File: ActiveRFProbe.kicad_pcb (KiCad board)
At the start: 2 copper layers, 49 x 22 mm, 40 parts, among them J1 Conn_01x01, J16 Conn_01x01, J17 Conn_01x01, J18 Conn_01x01, J19 Conn_01x01, J2 Conn_01x01, J20 Conn_01x01, J21 Conn_01x01, J22 Conn_01x01, J23 Conn_01x01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

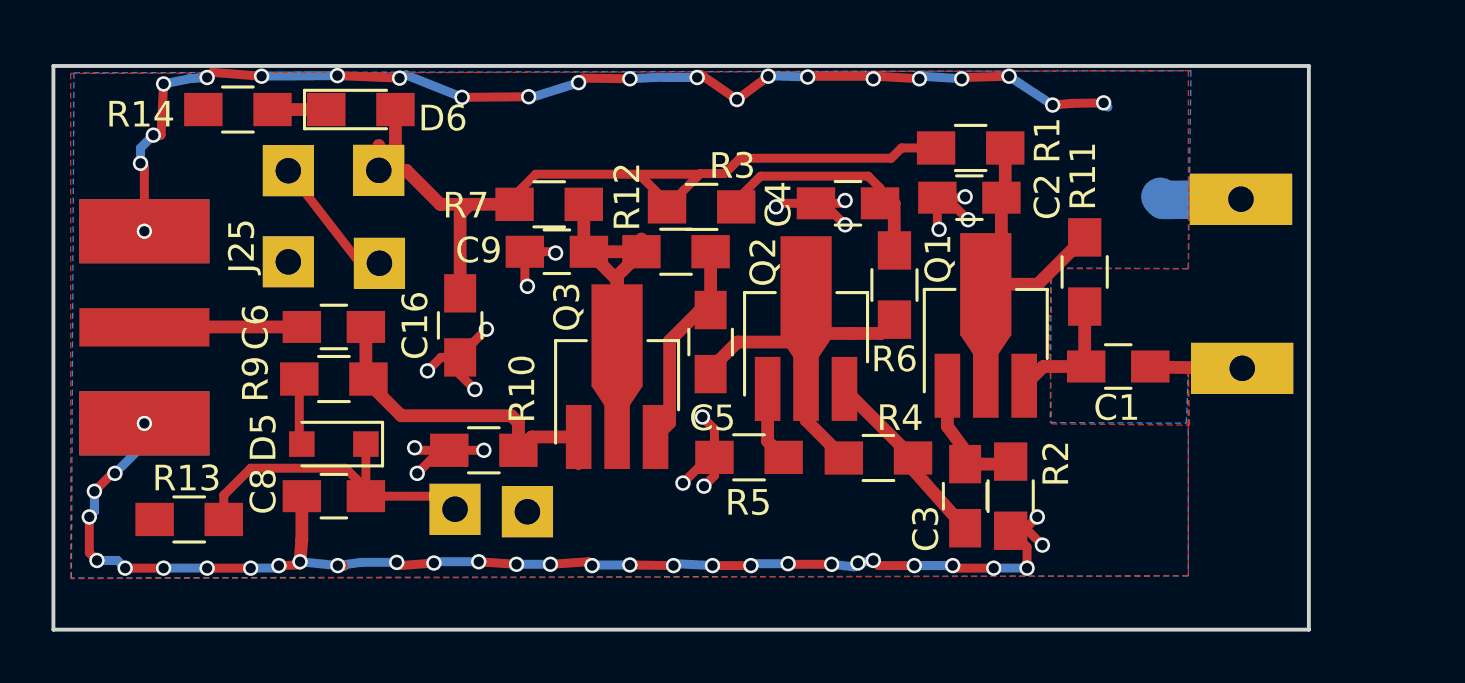
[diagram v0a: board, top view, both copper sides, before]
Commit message: Changed to 2SC3356
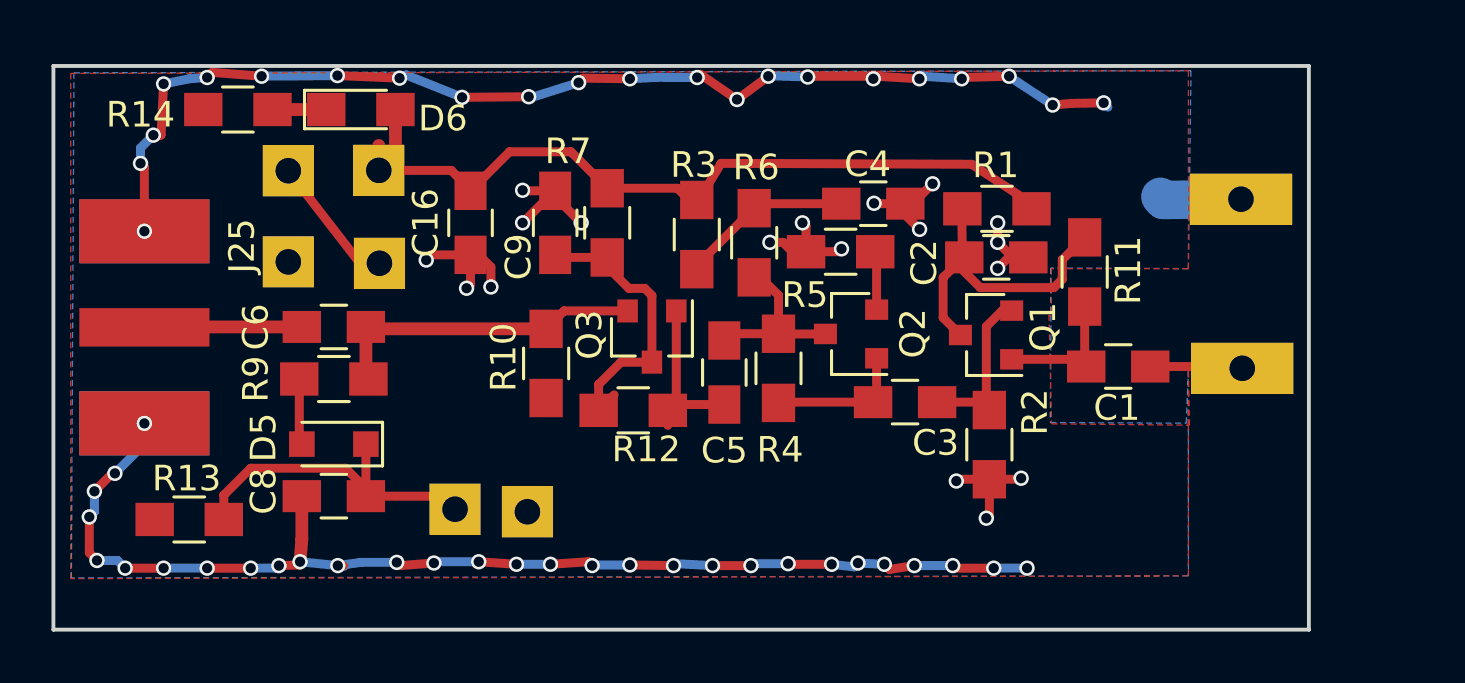
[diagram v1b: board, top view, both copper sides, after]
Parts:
- Q1, Q2, Q3: value 2SC1815 -> 2SC3356; footprint TO_SOT_Packages_SMD:SOT-89-3_Handsoldering -> TO_SOT_Packages_SMD:SOT-23
- moved R5 8.79 mm to (95.7, 88.2)
- moved R12 6.41 mm to (87.6, 94.4)
- moved R6 5.72 mm to (92.3, 87.9)
- moved R4 5.24 mm to (93.3, 92.8), turned to 270 degrees
- moved C3 4.35 mm to (98.2, 94.1), turned to 0 degrees
- moved R10 4.17 mm to (84.2, 92.6), turned to 270 degrees
- moved C16 4.02 mm to (81.3, 87.1)
- moved R1 2.59 mm to (101.8, 86.6), turned to 0 degrees
- moved C2 2.56 mm to (101.8, 88.5), turned to 180 degrees
- moved R7 2.38 mm to (86.6, 87.1), turned to 90 degrees
- moved Q3 2.37 mm to (88.4, 91.6), turned to 270 degrees
- moved R2 2.18 mm to (101.5, 95.8)
- moved Q2 1.76 mm to (96.1, 91.5), turned to 180 degrees
- moved C5 1.30 mm to (91.2, 93.0), turned to 90 degrees
- moved C9 1.13 mm to (84.6, 87.1), turned to 270 degrees
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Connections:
- Q1 pad 1: Net-(C3-Pad2) -> Net-(C1-Pad1)
- Q1 pad 2: Net-(C2-Pad2) -> Net-(C3-Pad2)
- Q1 pad 3: Net-(C1-Pad1) -> Net-(C2-Pad2)
- Q2 pad 1: Net-(Q2-Pad1) -> Net-(C3-Pad1)
- Q2 pad 2: Net-(C5-Pad2) -> Net-(Q2-Pad2)
- Q2 pad 3: Net-(C3-Pad1) -> Net-(C5-Pad2)
- Q3 pad 1: Net-(C6-Pad2) -> Net-(C5-Pad1)
- Q3 pad 2: Net-(C9-Pad2) -> Net-(C6-Pad2)
- Q3 pad 3: Net-(C5-Pad1) -> Net-(C9-Pad2)
- R5 pad 2: Net-(Q2-Pad1) -> Net-(Q2-Pad2)
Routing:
- net Net-(C5-Pad2): track 15.7 -> 6.80 mm
- net Net-(C9-Pad2): track 18.7 -> 11.6 mm
- net Net-(Q2-Pad1): track 4.12 -> 0.00 mm
- net Net-(C2-Pad2): track 17.2 -> 13.3 mm
- net Net-(C4-Pad1): track 10.4 -> 7.24 mm
- net Net-(C5-Pad1): track 9.39 -> 7.04 mm
- net Net-(Q2-Pad2): track 0.00 -> 2.28 mm
- net Net-(C3-Pad1): track 7.60 -> 5.47 mm
- net +9V: track 34.2 -> 32.1 mm
- net Net-(C3-Pad2): track 5.11 -> 6.87 mm
- net Net-(C6-Pad2): track 14.0 -> 13.0 mm
- net GND: track 124.6 -> 124.2 mm, vias 71 -> 70

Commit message: Added LCSC part numbers, added cutout notched, added series base resistors to emitter followers
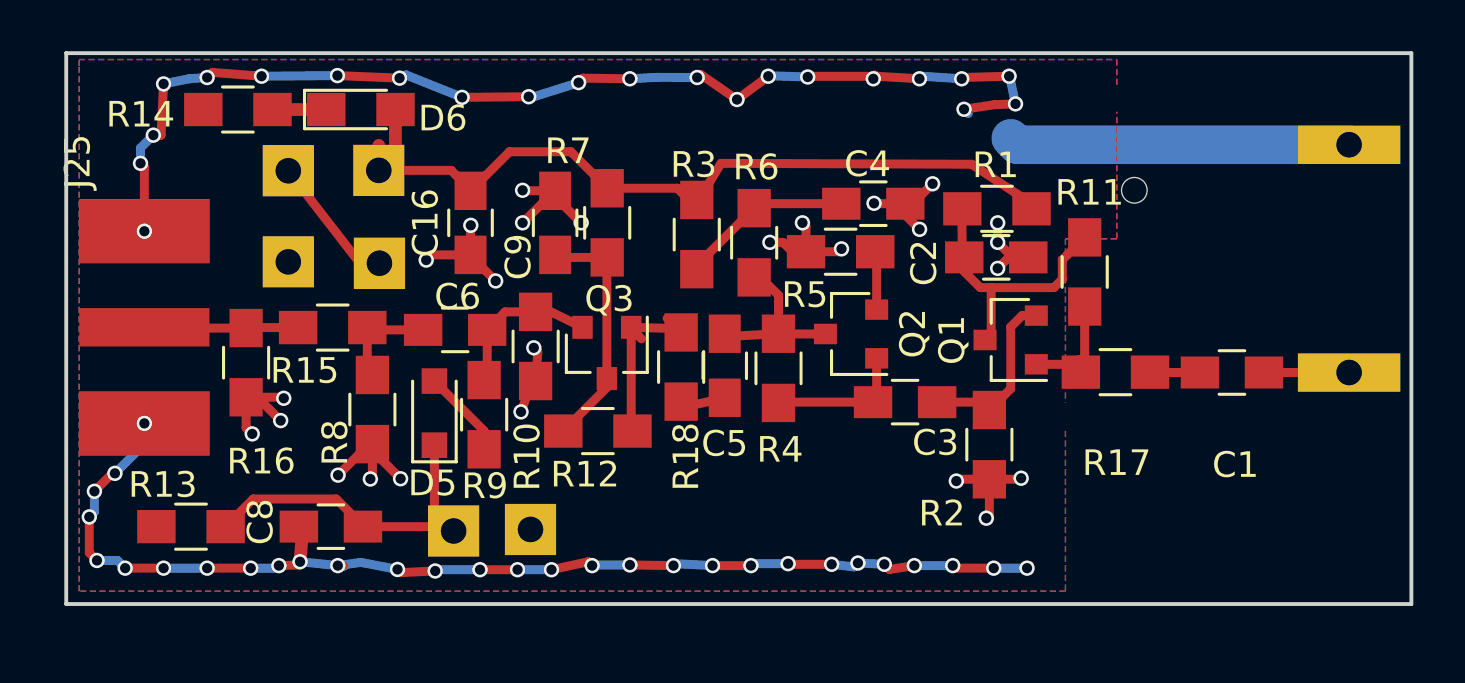
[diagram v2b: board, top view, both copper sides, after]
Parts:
- added J10: Conn_01x01, ActiveRFProbe:BigSlot, F.Cu at (111.2, 82.3)
- added J11: Conn_01x01, ActiveRFProbe:BigSlot, F.Cu at (106.0, 82.3)
- added J12: Conn_01x01, ActiveRFProbe:BigSlot, F.Cu at (107.2, 85.9)
- added J13: Conn_01x01, ActiveRFProbe:BigSlot, F.Cu at (115.8, 90.9)
- added J14: Conn_01x01, ActiveRFProbe:BigSlot, F.Cu at (115.6, 94.7)
- added J15: Conn_01x01, ActiveRFProbe:BigSlot, F.Cu at (115.9, 86.0)
- added J26: Conn_01x01, ActiveRFProbe:BigSlot, F.Cu at (115.9, 82.3)
- added J4: Conn_01x01, ActiveRFProbe:BigSlot, F.Cu at (111.2, 94.6)
- added J5: Conn_01x01, ActiveRFProbe:BigSlot, F.Cu at (105.8, 94.6)
- added J6: Conn_01x01, ActiveRFProbe:BigSlot, F.Cu at (103.9, 98.0)
- added J7: Conn_01x01, ActiveRFProbe:BigSlot, F.Cu at (110.9, 90.9)
- added J8: Conn_01x01, ActiveRFProbe:BigSlot, F.Cu at (111.0, 85.8)
- added J9: Conn_01x01, ActiveRFProbe:BigSlot, F.Cu at (107.2, 89.1)
- added R15: 0R, Resistors_SMD:R_0805_HandSoldering, F.Cu at (75.9, 91.2)
- added R16: NC, Resistors_SMD:R_0805_HandSoldering, F.Cu at (72.5, 92.6)
- added R17: 220R, Resistors_SMD:R_0805_HandSoldering, F.Cu at (106.5, 93.0)
- added R18: 220R, Resistors_SMD:R_0805_HandSoldering, F.Cu at (89.5, 92.8)
- added R8: NC, Resistors_SMD:R_0805_HandSoldering, F.Cu at (77.5, 94.4)
- R13: value 10k -> 100k
- moved R9 6.03 mm to (81.8, 94.6), turned to 90 degrees
- moved C6 4.74 mm to (80.7, 91.3)
- moved J16 4.73 mm to (115.6, 84.1)
- moved C1 4.44 mm to (111.0, 93.0)
- moved J1 4.17 mm to (115.6, 93.0)
- moved D5 4.11 mm to (79.9, 94.5), turned to 90 degrees
- moved Q3 1.87 mm to (86.6, 92.2)
- moved R12 1.60 mm to (86.2, 95.2)
- moved C8 1.20 mm to (75.8, 99.0)
- moved Q1 0.98 mm to (102.4, 91.7)
- moved J17 0.85 mm to (80.6, 99.2)
- moved R10 0.78 mm to (83.8, 91.9)
- moved J24 0.70 mm to (83.6, 99.1)
- moved R13 0.29 mm to (70.4, 99.0)
- moved C5 0.26 mm to (91.2, 92.7)
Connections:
- J25 pad 1: Net-(C6-Pad1) -> Net-(J25-Pad1)
- Q1 pad 1: Net-(C1-Pad1) -> Net-(Q1-Pad1)
- Q3 pad 1: Net-(C5-Pad1) -> Net-(Q3-Pad1)
- R11 pad 1: Net-(C1-Pad1) -> Net-(Q1-Pad1)
- R12 pad 1: Net-(C5-Pad1) -> Net-(Q3-Pad1)
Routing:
- net GND: track 124.2 -> 144.6 mm, vias 70 -> 78
- net Net-(Q3-Pad1): track 0.00 -> 7.48 mm
- net Net-(C6-Pad2): track 13.0 -> 6.62 mm
- net Net-(J25-Pad1): track 0.00 -> 6.06 mm
- net Net-(Q1-Pad1): track 0.00 -> 5.26 mm
- net Net-(C5-Pad1): track 7.04 -> 1.82 mm
- net Net-(C1-Pad1): track 5.90 -> 2.04 mm
- net Net-(C8-Pad2): track 13.3 -> 15.3 mm
- net Net-(C6-Pad1): track 6.17 -> 4.15 mm
- net Net-(C9-Pad2): track 11.6 -> 9.92 mm
- net Net-(C2-Pad2): track 13.3 -> 11.7 mm
- net Net-(D5-Pad2): track 2.58 -> 3.46 mm
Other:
- board size 49 x 22 mm -> 52.5 x 21.5 mm

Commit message: Modified base resistors
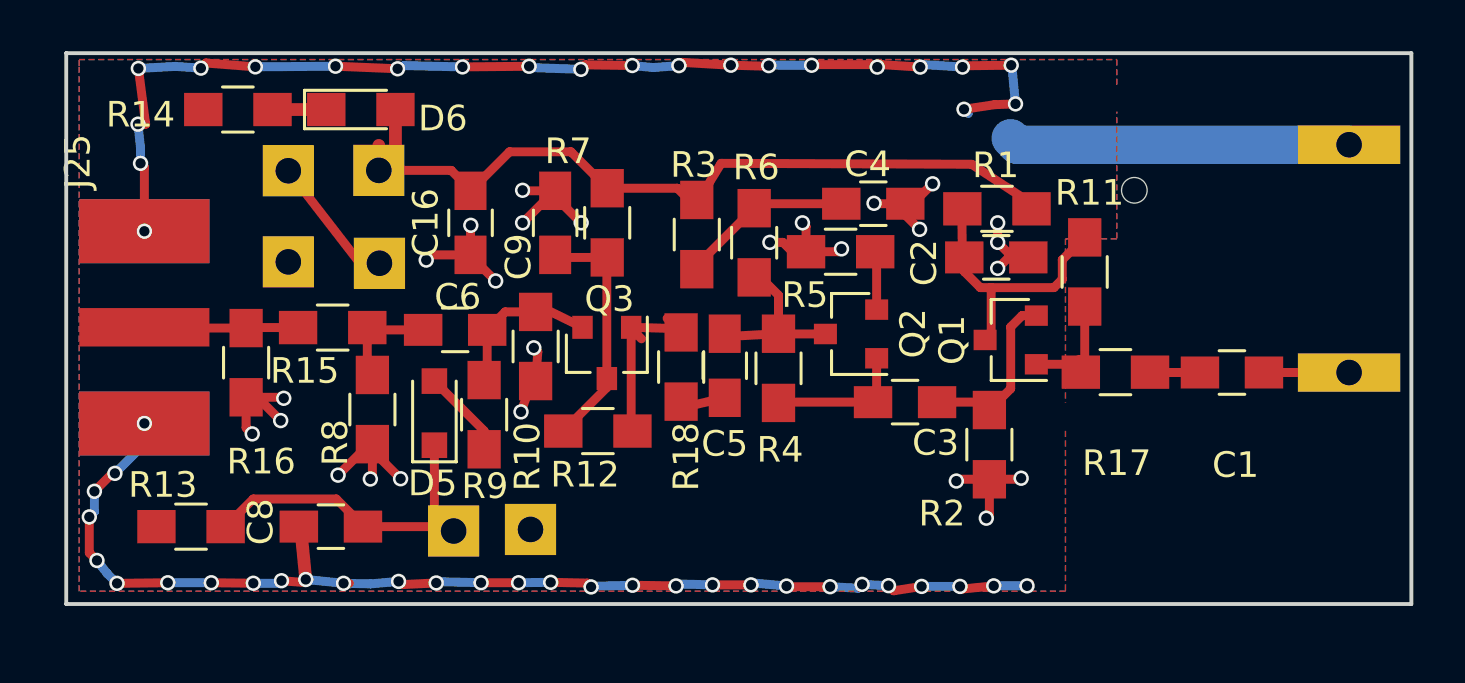
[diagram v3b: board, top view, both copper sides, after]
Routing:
- net GND: track 144.6 -> 146.6 mm
